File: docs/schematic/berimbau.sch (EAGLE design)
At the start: 54 parts, among them IC1 7805TV, IC2 LM386N-1, J1 P2_RPI, Q1 BD140, Q2 BD139, U1 ESP32-DEVKIT-C, U2 LMC6482, U3 APA3541

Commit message: added boot pull-down
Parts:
- added R20: 5k2, rcl:R-EU_0207/10
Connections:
- net GND: now also R20.2
- net URM_TRIGGER: now also R20.1
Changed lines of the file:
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@@
 <part name="R18" library="rcl" library_urn="urn:adsk.eagle:library:334" deviceset="R-EU_" device="0207/10" package3d_urn="urn:adsk.eagle:package:23491/2" value="100R"/>
 <part name="R19" library="rcl" library_urn="urn:adsk.eagle:library:334" deviceset="R-EU_" device="0207/10" package3d_urn="urn:adsk.eagle:package:23491/2" value="100R"/>
+<part name="R20" library="rcl" library_urn="urn:adsk.eagle:library:334" deviceset="R-EU_" device="0207/10" package3d_urn="urn:adsk.eagle:package:23491/2" value="5k2"/>
+<part name="GND26" library="supply1" library_urn="urn:adsk.eagle:library:371" deviceset="GND" device=""/>
 </parts>
 <sheets>
@@
 <attribute name="VALUE" x="115.57" y="39.878" size="1.778" layer="96"/>
 </instance>
+<instance part="R20" gate="G$1" x="0" y="-50.8" smashed="yes" rot="R180">
+<attribute name="NAME" x="3.81" y="-52.2986" size="1.778" layer="95" rot="R180"/>
+<attribute name="VALUE" x="3.81" y="-47.498" size="1.778" layer="96" rot="R180"/>
+</instance>
+<instance part="GND26" gate="1" x="-12.7" y="-55.88" smashed="yes">
+<attribute name="VALUE" x="-15.24" y="-58.42" size="1.778" layer="96"/>
+</instance>
 </instances>
 <busses>
@@
 <pinref part="A10" gate="G$1" pin="COMP/TRIG"/>
 <wire x1="10.16" y1="-38.1" x2="10.16" y2="-43.18" width="0.1524" layer="91"/>
-<wire x1="10.16" y1="-43.18" x2="5.08" y2="-43.18" width="0.1524" layer="91"/>
-<label x="5.08" y="-43.18" size="1.778" layer="95" rot="R180" xref="yes"/>
+<wire x1="10.16" y1="-43.18" x2="-5.08" y2="-43.18" width="0.1524" layer="91"/>
+<label x="-2.54" y="-43.18" size="1.778" layer="95" rot="R180" xref="yes"/>
+<wire x1="10.16" y1="-43.18" x2="10.16" y2="-50.8" width="0.1524" layer="91"/>
+<junction x="10.16" y="-43.18"/>
+<pinref part="R20" gate="G$1" pin="1"/>
+<wire x1="10.16" y1="-50.8" x2="5.08" y2="-50.8" width="0.1524" layer="91"/>
 </segment>
 </net>
@@
 <junction x="127" y="43.18"/>
 </segment>
-</net>
+<segment>
+<pinref part="R20" gate="G$1" pin="2"/>
+<wire x1="-5.08" y1="-50.8" x2="-12.7" y2="-50.8" width="0.1524" layer="91"/>
+<wire x1="-12.7" y1="-50.8" x2="-12.7" y2="-53.34" width="0.1524" layer="91"/>
+<pinref part="GND26" gate="1" pin="GND"/>
+</segment>
+</net>

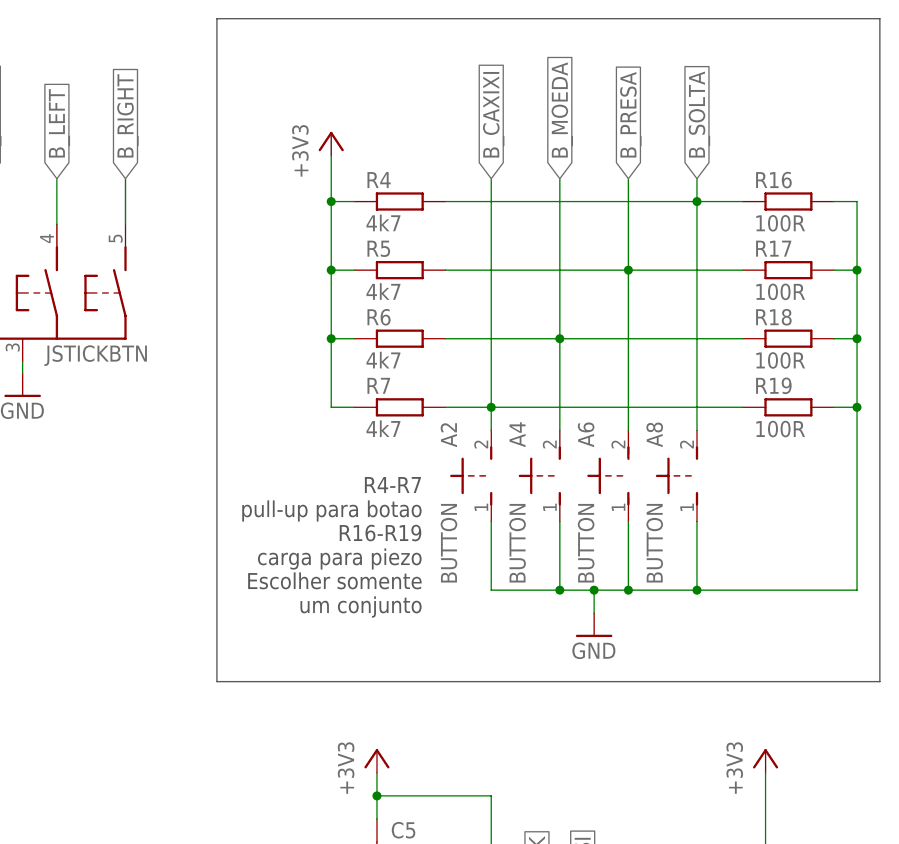
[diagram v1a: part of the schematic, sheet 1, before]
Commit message: removed pull down on piezo
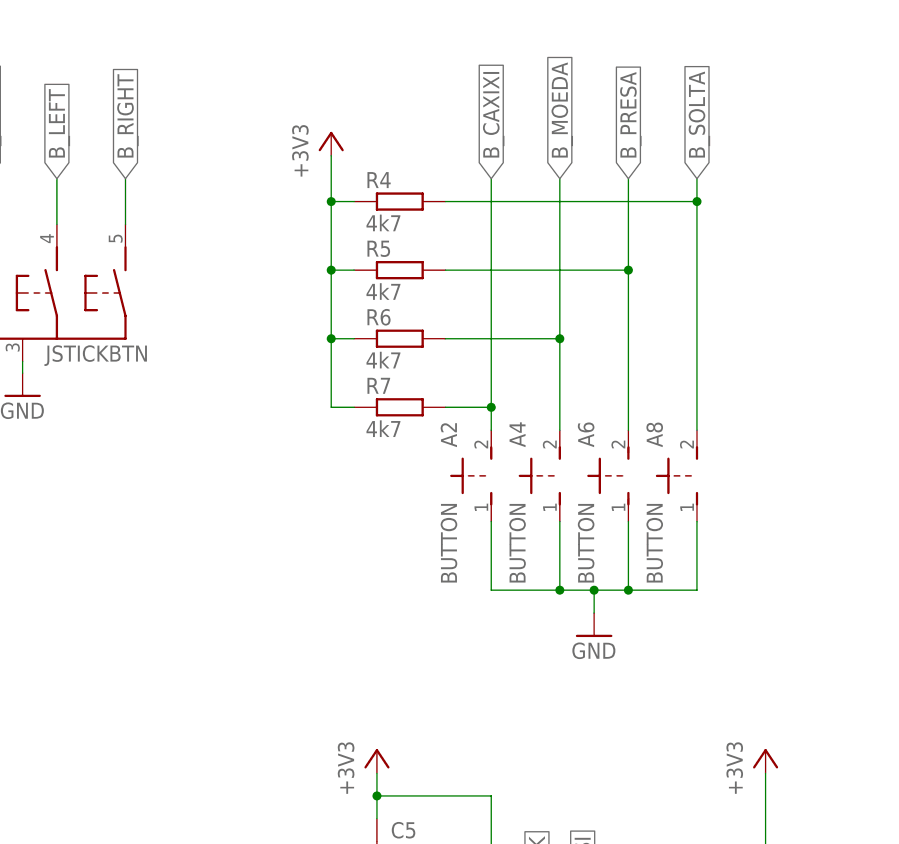
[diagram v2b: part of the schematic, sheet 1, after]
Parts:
- removed R16, R17, R18, R19: 100R, rcl:R-EU_0207/10
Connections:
- net B_CAXIXI: no longer R19.1
- net B_MOEDA: no longer R18.1
- net B_PRESA: no longer R17.1
- net B_SOLTA: no longer R16.1
- net GND: no longer R16.2, R17.2, R18.2, R19.2
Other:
- note removed: "R4-R7 pull-up para botao R16-R19 carga para piezo Escolher somente um conjunto"
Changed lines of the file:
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@@
 <?xml version="1.0" encoding="utf-8"?>
 <!DOCTYPE eagle SYSTEM "eagle.dtd">
-<eagle version="9.3.1">
+<eagle version="9.4.0">
 <drawing>
 <settings>
@@
 <part name="U1" library="angelo" deviceset="ESP32-DEVKIT-C" device=""/>
 <part name="GND3" library="supply1" library_urn="urn:adsk.eagle:library:371" deviceset="GND" device=""/>
-<part name="R16" library="rcl" library_urn="urn:adsk.eagle:library:334" deviceset="R-EU_" device="0207/10" package3d_urn="urn:adsk.eagle:package:23491/2" value="100R"/>
-<part name="R17" library="rcl" library_urn="urn:adsk.eagle:library:334" deviceset="R-EU_" device="0207/10" package3d_urn="urn:adsk.eagle:package:23491/2" value="100R"/>
-<part name="R18" library="rcl" library_urn="urn:adsk.eagle:library:334" deviceset="R-EU_" device="0207/10" package3d_urn="urn:adsk.eagle:package:23491/2" value="100R"/>
-<part name="R19" library="rcl" library_urn="urn:adsk.eagle:library:334" deviceset="R-EU_" device="0207/10" package3d_urn="urn:adsk.eagle:package:23491/2" value="100R"/>
 <part name="R20" library="rcl" library_urn="urn:adsk.eagle:library:334" deviceset="R-EU_" device="0207/10" package3d_urn="urn:adsk.eagle:package:23491/2" value="5k2"/>
 <part name="GND26" library="supply1" library_urn="urn:adsk.eagle:library:371" deviceset="GND" device=""/>
@@
 GEPID - Grupo de Pesquisa em Cultura Digital
 UPF (Universidade de Passo Fundo) - upf.br</text>
-<text x="78.74" y="20.32" size="1.778" layer="97" rot="MR0">R4-R7
-pull-up para botao
-R16-R19
-carga para piezo
-Escolher somente
-um conjunto</text>
-<wire x1="55.88" y1="86.36" x2="55.88" y2="12.7" width="0.1524" layer="97"/>
-<wire x1="55.88" y1="12.7" x2="129.54" y2="12.7" width="0.1524" layer="97"/>
-<wire x1="129.54" y1="12.7" x2="129.54" y2="86.36" width="0.1524" layer="97"/>
-<wire x1="129.54" y1="86.36" x2="55.88" y2="86.36" width="0.1524" layer="97"/>
 </plain>
 <instances>
@@
 <attribute name="VALUE" x="-78.74" y="-17.78" size="1.778" layer="96"/>
 </instance>
-<instance part="R16" gate="G$1" x="119.38" y="66.04" smashed="yes">
-<attribute name="NAME" x="115.57" y="67.5386" size="1.778" layer="95"/>
-<attribute name="VALUE" x="115.57" y="62.738" size="1.778" layer="96"/>
-</instance>
-<instance part="R17" gate="G$1" x="119.38" y="58.42" smashed="yes">
-<attribute name="NAME" x="115.57" y="59.9186" size="1.778" layer="95"/>
-<attribute name="VALUE" x="115.57" y="55.118" size="1.778" layer="96"/>
-</instance>
-<instance part="R18" gate="G$1" x="119.38" y="50.8" smashed="yes">
-<attribute name="NAME" x="115.57" y="52.2986" size="1.778" layer="95"/>
-<attribute name="VALUE" x="115.57" y="47.498" size="1.778" layer="96"/>
-</instance>
-<instance part="R19" gate="G$1" x="119.38" y="43.18" smashed="yes">
-<attribute name="NAME" x="115.57" y="44.6786" size="1.778" layer="95"/>
-<attribute name="VALUE" x="115.57" y="39.878" size="1.778" layer="96"/>
-</instance>
 <instance part="R20" gate="G$1" x="0" y="-50.8" smashed="yes" rot="R180">
 <attribute name="NAME" x="3.81" y="-52.2986" size="1.778" layer="95" rot="R180"/>
@@
 <wire x1="93.98" y1="50.8" x2="93.98" y2="68.58" width="0.1524" layer="91"/>
 <junction x="93.98" y="50.8"/>
-<wire x1="114.3" y1="50.8" x2="93.98" y2="50.8" width="0.1524" layer="91"/>
 <label x="93.98" y="68.58" size="1.778" layer="95" rot="R90" xref="yes"/>
-<pinref part="R18" gate="G$1" pin="1"/>
 </segment>
 </net>
@@
 <wire x1="86.36" y1="43.18" x2="86.36" y2="68.58" width="0.1524" layer="91"/>
 <junction x="86.36" y="43.18"/>
-<wire x1="114.3" y1="43.18" x2="86.36" y2="43.18" width="0.1524" layer="91"/>
 <label x="86.36" y="68.58" size="1.778" layer="95" rot="R90" xref="yes"/>
-<pinref part="R19" gate="G$1" pin="1"/>
 </segment>
 </net>
@@
 <wire x1="101.6" y1="58.42" x2="101.6" y2="68.58" width="0.1524" layer="91"/>
 <junction x="101.6" y="58.42"/>
-<wire x1="114.3" y1="58.42" x2="101.6" y2="58.42" width="0.1524" layer="91"/>
 <label x="101.6" y="68.58" size="1.778" layer="95" rot="R90" xref="yes"/>
-<pinref part="R17" gate="G$1" pin="1"/>
 </segment>
 </net>
@@
 <wire x1="109.22" y1="66.04" x2="109.22" y2="68.58" width="0.1524" layer="91"/>
 <junction x="109.22" y="66.04"/>
-<wire x1="114.3" y1="66.04" x2="109.22" y2="66.04" width="0.1524" layer="91"/>
 <label x="109.22" y="68.58" size="1.778" layer="95" rot="R90" xref="yes"/>
-<pinref part="R16" gate="G$1" pin="1"/>
 </segment>
 </net>
@@
 <wire x1="109.22" y1="22.86" x2="101.6" y2="22.86" width="0.1524" layer="91"/>
 <junction x="101.6" y="22.86"/>
-<wire x1="127" y1="22.86" x2="109.22" y2="22.86" width="0.1524" layer="91"/>
-<junction x="109.22" y="22.86"/>
 <pinref part="GND18" gate="1" pin="GND"/>
 <wire x1="97.79" y1="20.32" x2="97.79" y2="22.86" width="0.1524" layer="91"/>
 <junction x="97.79" y="22.86"/>
-<pinref part="R16" gate="G$1" pin="2"/>
-<wire x1="124.46" y1="66.04" x2="127" y2="66.04" width="0.1524" layer="91"/>
-<wire x1="127" y1="66.04" x2="127" y2="58.42" width="0.1524" layer="91"/>
-<pinref part="R17" gate="G$1" pin="2"/>
-<wire x1="127" y1="58.42" x2="124.46" y2="58.42" width="0.1524" layer="91"/>
-<pinref part="R18" gate="G$1" pin="2"/>
-<wire x1="124.46" y1="50.8" x2="127" y2="50.8" width="0.1524" layer="91"/>
-<wire x1="127" y1="50.8" x2="127" y2="58.42" width="0.1524" layer="91"/>
-<junction x="127" y="58.42"/>
-<pinref part="R19" gate="G$1" pin="2"/>
-<wire x1="124.46" y1="43.18" x2="127" y2="43.18" width="0.1524" layer="91"/>
-<wire x1="127" y1="43.18" x2="127" y2="50.8" width="0.1524" layer="91"/>
-<junction x="127" y="50.8"/>
-<wire x1="127" y1="22.86" x2="127" y2="43.18" width="0.1524" layer="91"/>
-<junction x="127" y="43.18"/>
-</segment>
-<segment>
+</segment>
+<segment>
